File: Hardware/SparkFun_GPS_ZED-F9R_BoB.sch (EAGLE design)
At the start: 72 parts, among them J1 U.FL, J3 QWIIC_RIGHT_ANGLE, J4 QWIIC_RIGHT_ANGLE, U1 HCPL-073L, U2 UBLOX_ZED_F9R, U3 UHS_INVERTER_SCHMITT_TRIGGERS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, U4 UHS_INVERTER_SCHMITT_TRIGGERS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, U5 3.3V

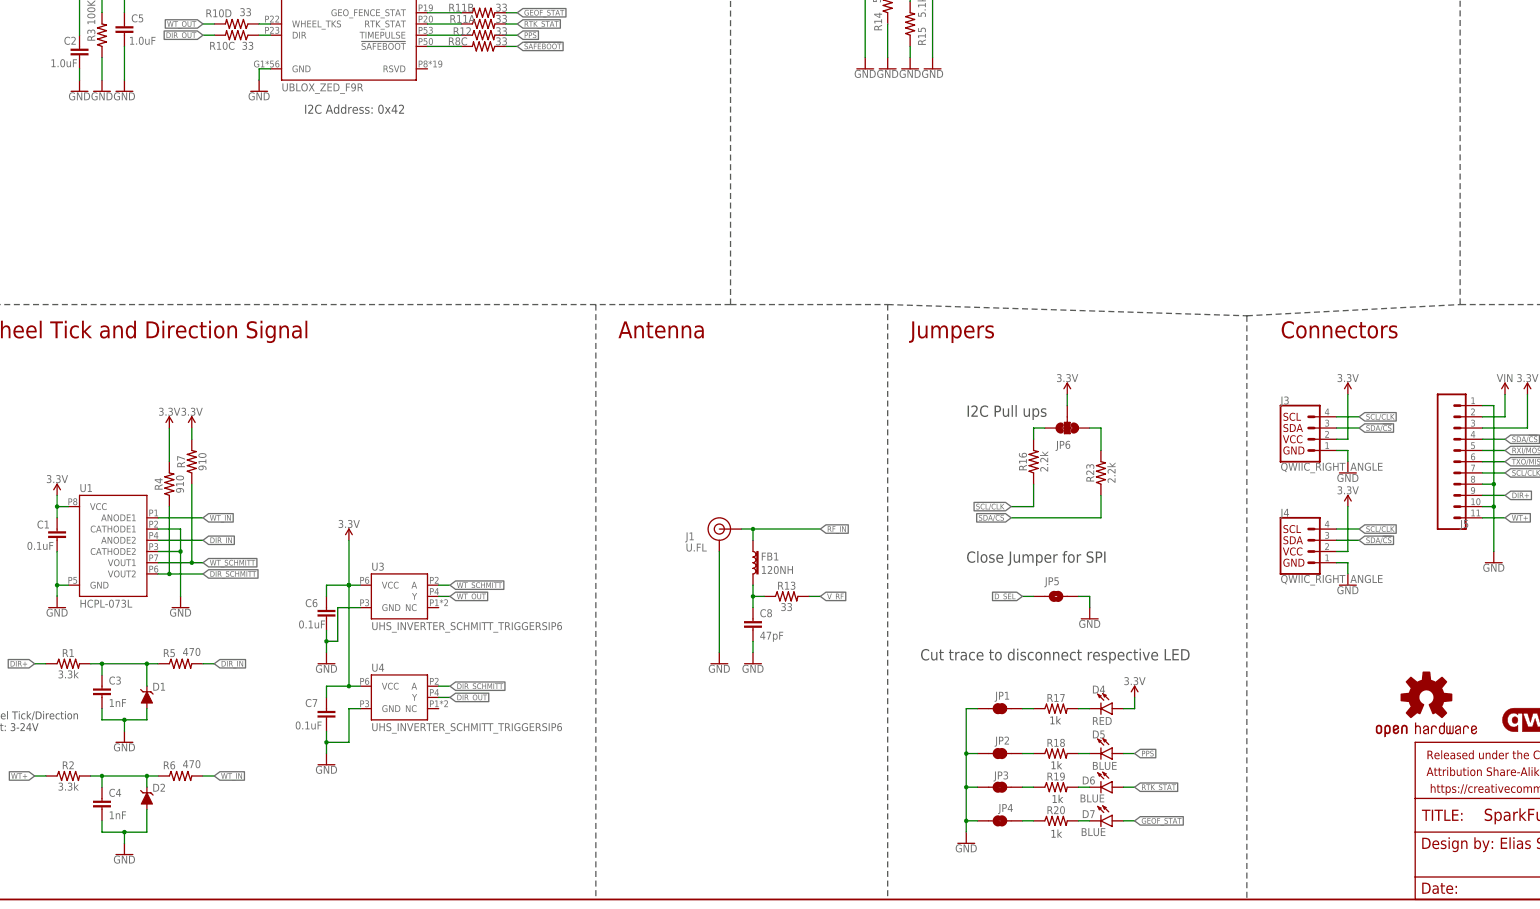
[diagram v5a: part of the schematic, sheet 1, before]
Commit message: Updates all parts to parts in Eagle Libraries
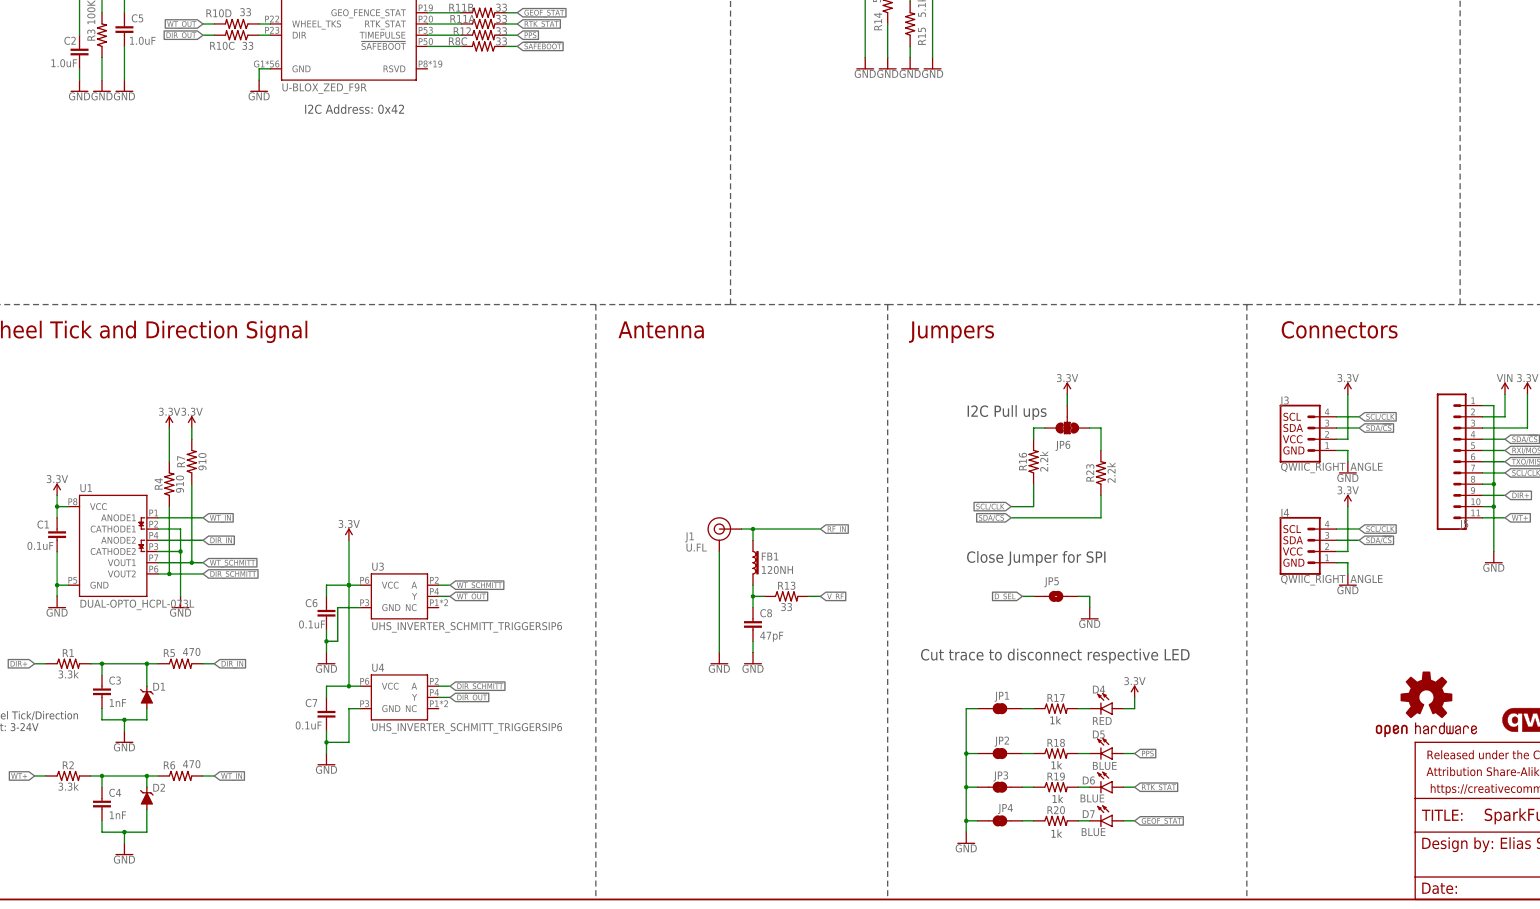
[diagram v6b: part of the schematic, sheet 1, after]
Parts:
- D1, D2: value 0.5A/40V/420mV -> 15V; device classified:BZX84_DIODE -> SparkFun-DiscreteSemi:DIODE-ZENER-BZX84C15LT3G
- R10, R11, R8, R9: device SparkFun-Resistors:33OHM_RESISTOR_ARRAY -> SparkFun-Resistors:33OHM_RA-1206-1/16W-5%
- U1: value HCPL-073L -> DUAL-OPTO_HCPL-073L; device classified:HCPL-073L -> SparkFun-DiscreteSemi:DUAL-OPTO_HCPL-073L
- U2: value UBLOX_ZED_F9R -> U-BLOX_ZED_F9R; device classified:UBLOX_ZED_F9R -> SparkFun-GPS:U-BLOX_ZED_F9R
- U3, U4: device classified:UHS_INVERTER_SCHMITT_TRIGGERSIP6 -> SparkFun-IC-Amplifiers:UHS_INVERTER_SCHMITT_TRIGGERSIP6
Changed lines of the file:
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@@
 <part name="GND1" library="SparkFun-PowerSymbols" deviceset="GND" device=""/>
 <part name="SUPPLY1" library="SparkFun-PowerSymbols" deviceset="V_BATT" device=""/>
-<part name="U2" library="classified" deviceset="UBLOX_ZED_F9R" device=""/>
+<part name="U2" library="SparkFun-GPS" deviceset="U-BLOX_ZED_F9R" device=""/>
 <part name="C2" library="SparkFun-Capacitors" deviceset="1.0UF" device="-0603-16V-10%-X7R" value="1.0uF"/>
 <part name="SUPPLY3" library="SparkFun-PowerSymbols" deviceset="3.3V" device=""/>
@@
 <part name="C3" library="SparkFun-Capacitors" deviceset="1.0NF/1000PF" device="-0402-25V-10%-X7R" value="1nF"/>
 <part name="C4" library="SparkFun-Capacitors" deviceset="1.0NF/1000PF" device="-0402-25V-10%-X7R" value="1nF"/>
-<part name="D2" library="classified" deviceset="BZX84_DIODE" device="" value="0.5A/40V/420mV"/>
+<part name="D2" library="SparkFun-DiscreteSemi" deviceset="DIODE-ZENER" device="-BZX84C15LT3G" value="15V"/>
 <part name="R7" library="classified" deviceset="910OHM-0603-1/10W-5%" device="" value="910"/>
 <part name="R4" library="classified" deviceset="910OHM-0603-1/10W-5%" device="" value="910"/>
-<part name="U1" library="classified" deviceset="HCPL-073L" device=""/>
+<part name="U1" library="SparkFun-DiscreteSemi" deviceset="DUAL-OPTO_HCPL-073L" device=""/>
 <part name="C1" library="SparkFun-Capacitors" deviceset="0.1UF" device="-0402-6.3V-10%-X7R" value="0.1uF"/>
 <part name="SUPPLY21" library="SparkFun-PowerSymbols" deviceset="3.3V" device=""/>
 <part name="GND25" library="SparkFun-PowerSymbols" deviceset="GND" device=""/>
-<part name="U3" library="classified" deviceset="UHS_INVERTER_SCHMITT_TRIGGER" device="SIP6" value="UHS_INVERTER_SCHMITT_TRIGGERSIP6"/>
-<part name="U4" library="classified" deviceset="UHS_INVERTER_SCHMITT_TRIGGER" device="SIP6" value="UHS_INVERTER_SCHMITT_TRIGGERSIP6"/>
+<part name="U3" library="SparkFun-IC-Amplifiers" deviceset="UHS_INVERTER_SCHMITT_TRIGGER" device="SIP6" value="UHS_INVERTER_SCHMITT_TRIGGERSIP6"/>
+<part name="U4" library="SparkFun-IC-Amplifiers" deviceset="UHS_INVERTER_SCHMITT_TRIGGER" device="SIP6" value="UHS_INVERTER_SCHMITT_TRIGGERSIP6"/>
 <part name="SUPPLY22" library="SparkFun-PowerSymbols" deviceset="3.3V" device=""/>
 <part name="GND26" library="SparkFun-PowerSymbols" deviceset="GND" device=""/>
-<part name="D1" library="classified" deviceset="BZX84_DIODE" device="" value="0.5A/40V/420mV"/>
+<part name="D1" library="SparkFun-DiscreteSemi" deviceset="DIODE-ZENER" device="-BZX84C15LT3G" value="15V"/>
 <part name="SUPPLY23" library="SparkFun-PowerSymbols" deviceset="3.3V" device=""/>
 <part name="SUPPLY24" library="SparkFun-PowerSymbols" deviceset="3.3V" device=""/>
@@
 <part name="GND22" library="SparkFun-PowerSymbols" deviceset="GND" device=""/>
 <part name="GND23" library="SparkFun-PowerSymbols" deviceset="GND" device=""/>
-<part name="R9" library="SparkFun-Resistors" deviceset="33OHM_RESISTOR_ARRAY" device="" value="33"/>
-<part name="R8" library="SparkFun-Resistors" deviceset="33OHM_RESISTOR_ARRAY" device="" value="33"/>
-<part name="R10" library="SparkFun-Resistors" deviceset="33OHM_RESISTOR_ARRAY" device="" value="33"/>
-<part name="R11" library="SparkFun-Resistors" deviceset="33OHM_RESISTOR_ARRAY" device="" value="33"/>
+<part name="R9" library="SparkFun-Resistors" deviceset="33OHM_RA" device="-1206-1/16W-5%" value="33"/>
+<part name="R8" library="SparkFun-Resistors" deviceset="33OHM_RA" device="-1206-1/16W-5%" value="33"/>
+<part name="R10" library="SparkFun-Resistors" deviceset="33OHM_RA" device="-1206-1/16W-5%" value="33"/>
+<part name="R11" library="SparkFun-Resistors" deviceset="33OHM_RA" device="-1206-1/16W-5%" value="33"/>
 </parts>
 <sheets>
@@
 Max Current: 600mA</text>
 <text x="180.34" y="269.24" size="3.81" layer="94" font="vector">Power</text>
-<wire x1="210.82" y1="134.62" x2="292.1" y2="132.08" width="0.1524" layer="97" style="shortdash"/>
-<wire x1="292.1" y1="132.08" x2="340.36" y2="134.62" width="0.1524" layer="97" style="shortdash"/>
+<wire x1="210.82" y1="134.62" x2="292.1" y2="134.62" width="0.1524" layer="97" style="shortdash"/>
+<wire x1="292.1" y1="134.62" x2="340.36" y2="134.62" width="0.1524" layer="97" style="shortdash"/>
 <wire x1="340.36" y1="134.62" x2="431.8" y2="134.62" width="0.1524" layer="97" style="shortdash"/>
 <wire x1="340.36" y1="279.4" x2="340.36" y2="134.62" width="0.2032" layer="97" style="shortdash"/>
 <text x="247.65" y="29.464" size="1.778" layer="97" font="vector">1k</text>
 <text x="247.904" y="21.844" size="1.778" layer="97" font="vector">1k</text>
-<wire x1="292.1" y1="132.08" x2="292.1" y2="0" width="0.2032" layer="97" style="shortdash"/>
+<wire x1="292.1" y1="134.62" x2="292.1" y2="0" width="0.2032" layer="97" style="shortdash"/>
 <text x="247.396" y="39.624" size="1.778" layer="97" font="vector">1k</text>
 <text x="73.66" y="241.3" size="2.032" layer="97" font="vector">VCC Range: 2.7V - 3.6V</text>

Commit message: Replaces 910 Ohm resistor with part in Eagle Library
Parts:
- R4, R7: device classified:910OHM-0603-1/10W-5% -> SparkFun-Resistors:910OHM-0603-1/10W-5%
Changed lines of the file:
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@@
 <part name="C4" library="SparkFun-Capacitors" deviceset="1.0NF/1000PF" device="-0402-25V-10%-X7R" value="1nF"/>
 <part name="D2" library="SparkFun-DiscreteSemi" deviceset="DIODE-ZENER" device="-BZX84C15LT3G" value="15V"/>
-<part name="R7" library="classified" deviceset="910OHM-0603-1/10W-5%" device="" value="910"/>
-<part name="R4" library="classified" deviceset="910OHM-0603-1/10W-5%" device="" value="910"/>
+<part name="R7" library="SparkFun-Resistors" deviceset="910OHM" device="-0603-1/10W-5%" value="910"/>
+<part name="R4" library="SparkFun-Resistors" deviceset="910OHM" device="-0603-1/10W-5%" value="910"/>
 <part name="U1" library="SparkFun-DiscreteSemi" deviceset="DUAL-OPTO_HCPL-073L" device=""/>
 <part name="C1" library="SparkFun-Capacitors" deviceset="0.1UF" device="-0402-6.3V-10%-X7R" value="0.1uF"/>

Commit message: Replaces 0.1uF 6.3V with the 0.1uF 10V X7R capacitors
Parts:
- C1, C6, C7: device SparkFun-Capacitors:0.1UF-0402-6.3V-10%-X7R -> SparkFun-Capacitors:0.1UF-0402-10V-10%-X7R
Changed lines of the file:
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@@
 <part name="R4" library="SparkFun-Resistors" deviceset="910OHM" device="-0603-1/10W-5%" value="910"/>
 <part name="U1" library="SparkFun-DiscreteSemi" deviceset="DUAL-OPTO_HCPL-073L" device=""/>
-<part name="C1" library="SparkFun-Capacitors" deviceset="0.1UF" device="-0402-6.3V-10%-X7R" value="0.1uF"/>
+<part name="C1" library="SparkFun-Capacitors" deviceset="0.1UF" device="-0402-10V-10%-X7R" value="0.1uF"/>
 <part name="SUPPLY21" library="SparkFun-PowerSymbols" deviceset="3.3V" device=""/>
 <part name="GND25" library="SparkFun-PowerSymbols" deviceset="GND" device=""/>
@@
 <part name="SUPPLY23" library="SparkFun-PowerSymbols" deviceset="3.3V" device=""/>
 <part name="SUPPLY24" library="SparkFun-PowerSymbols" deviceset="3.3V" device=""/>
-<part name="C6" library="SparkFun-Capacitors" deviceset="0.1UF" device="-0402-6.3V-10%-X7R" value="0.1uF"/>
-<part name="C7" library="SparkFun-Capacitors" deviceset="0.1UF" device="-0402-6.3V-10%-X7R" value="0.1uF"/>
+<part name="C6" library="SparkFun-Capacitors" deviceset="0.1UF" device="-0402-10V-10%-X7R" value="0.1uF"/>
+<part name="C7" library="SparkFun-Capacitors" deviceset="0.1UF" device="-0402-10V-10%-X7R" value="0.1uF"/>
 <part name="GND29" library="SparkFun-PowerSymbols" deviceset="GND" device=""/>
 <part name="C5" library="SparkFun-Capacitors" deviceset="1.0UF" device="-0603-16V-10%-X7R" value="1.0uF"/>
